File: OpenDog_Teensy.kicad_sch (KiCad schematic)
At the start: 42 parts

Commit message: Added input voltage monitoring cirquit.
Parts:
- added C: C, symbol Device:C
- added D: BAT54S, Package_TO_SOT_SMD:SOT-23, symbol Diode:BAT54S
- added R (x3): R, symbol Device:R
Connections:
- net 3.3V: now also D.2
- net GND: now also C.2, D.1, R.2
- net VIn: now also R.1
- net EXT8: no longer names the net of J.10 (Pin_10)
- net EXT8: no longer U.33 (41_A17)
- new net: C.1, D.3, R.1, R.2, R.2
- new net V_MON: R.1, U.33 (41_A17)
- no-connect marks 7 -> 8

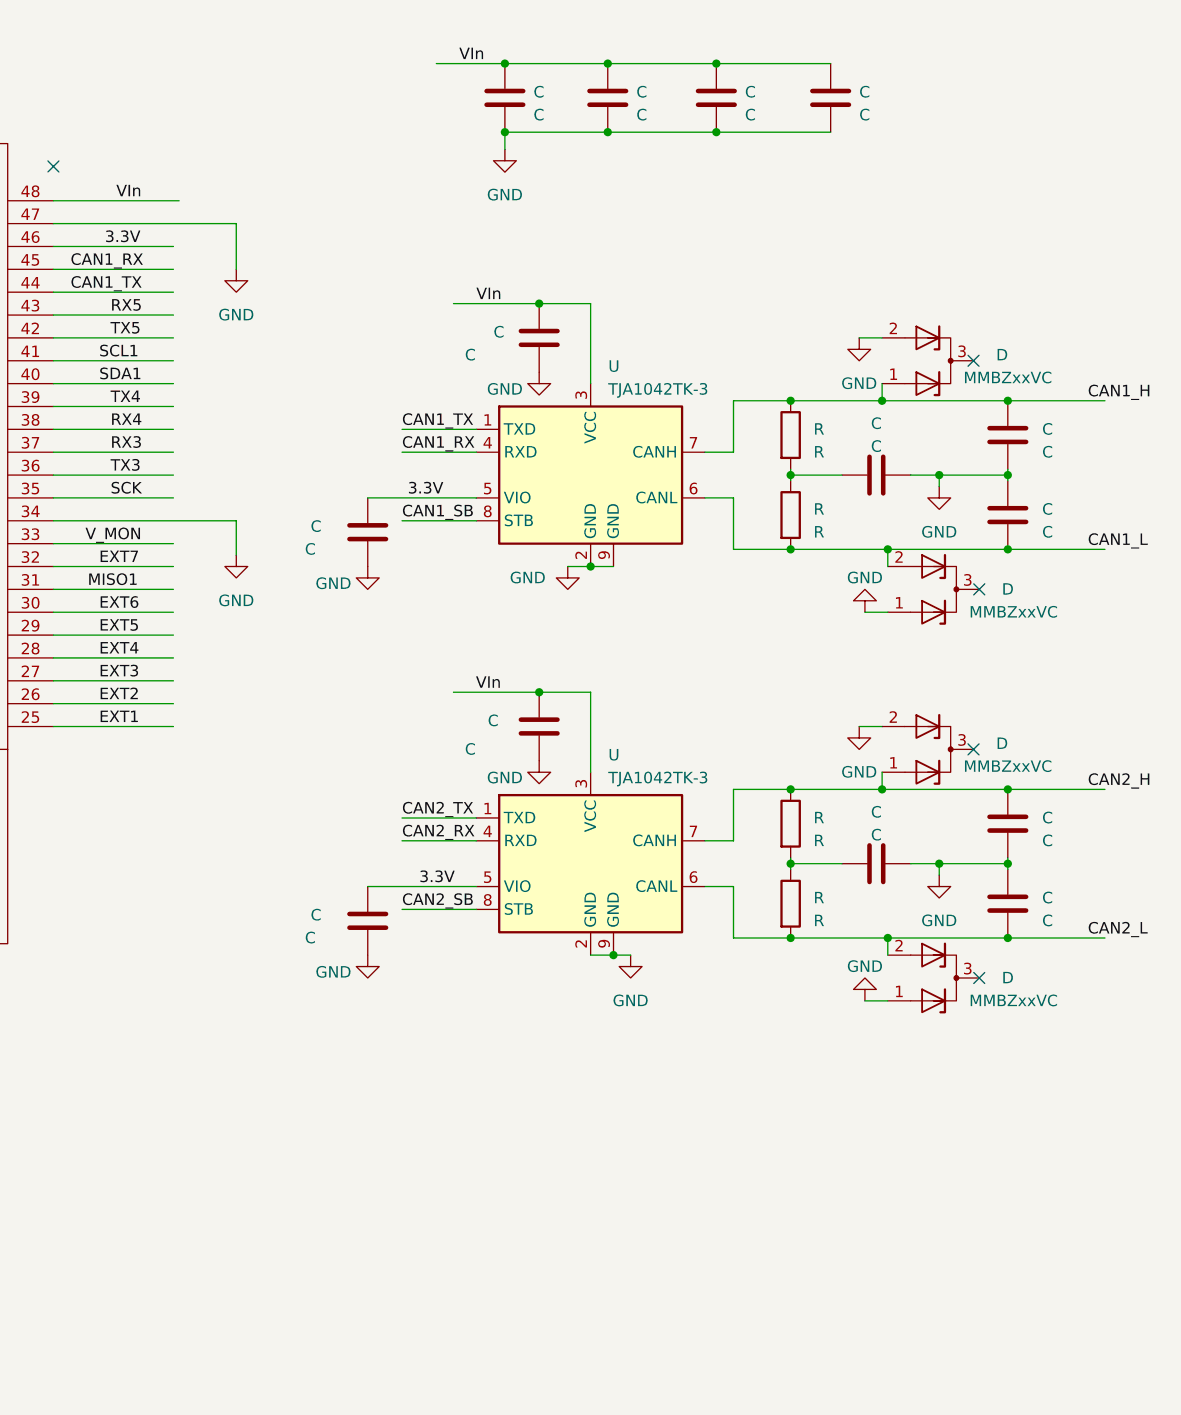
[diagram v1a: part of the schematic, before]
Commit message: Added more filtering capacitors on the 3.3v rail one for each connector.
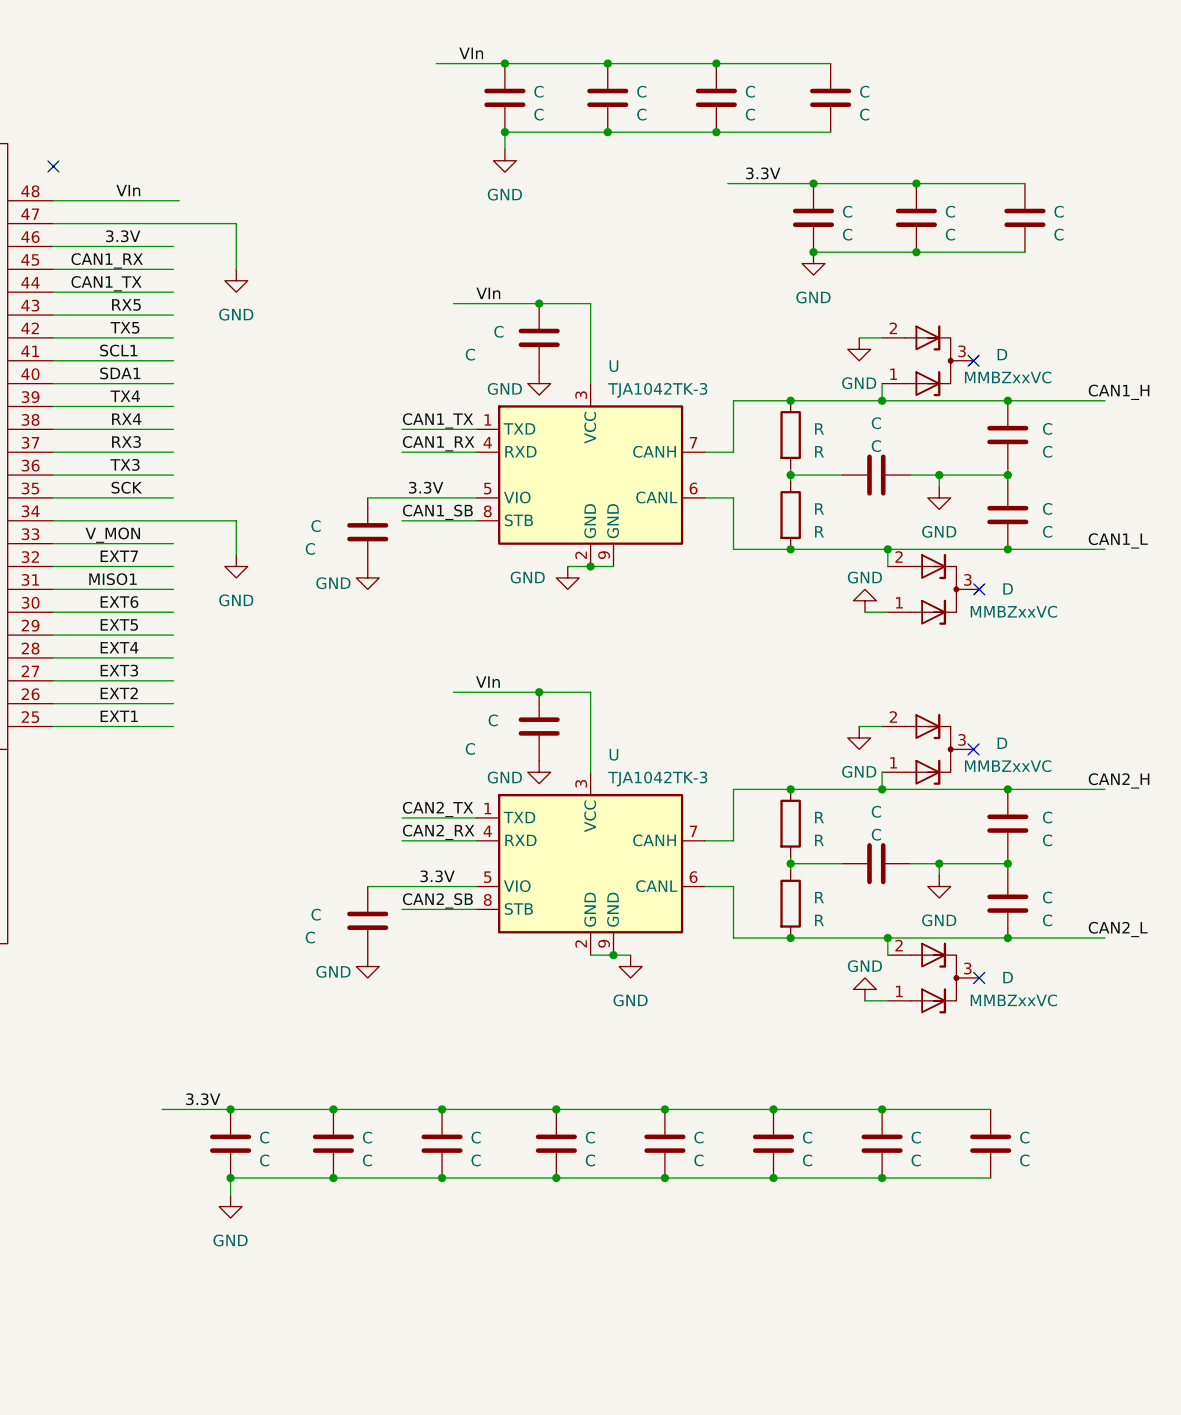
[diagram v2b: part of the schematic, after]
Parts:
- added C (x11): C, symbol Device:C
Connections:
- net 3.3V: now also C.1, C.1, C.1, C.1, C.1, C.1, C.1, C.1, C.1, C.1, C.1
- net GND: now also C.2, C.2, C.2, C.2, C.2, C.2, C.2, C.2, C.2, C.2, C.2

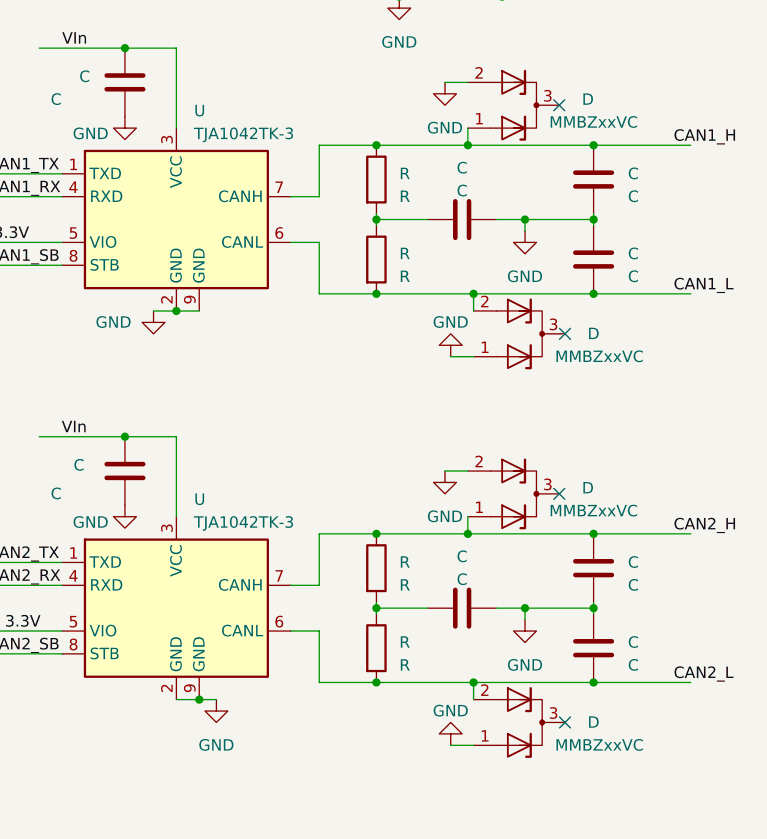
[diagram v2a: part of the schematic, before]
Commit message: Update OpenDog board part numbers. Small routing changes.
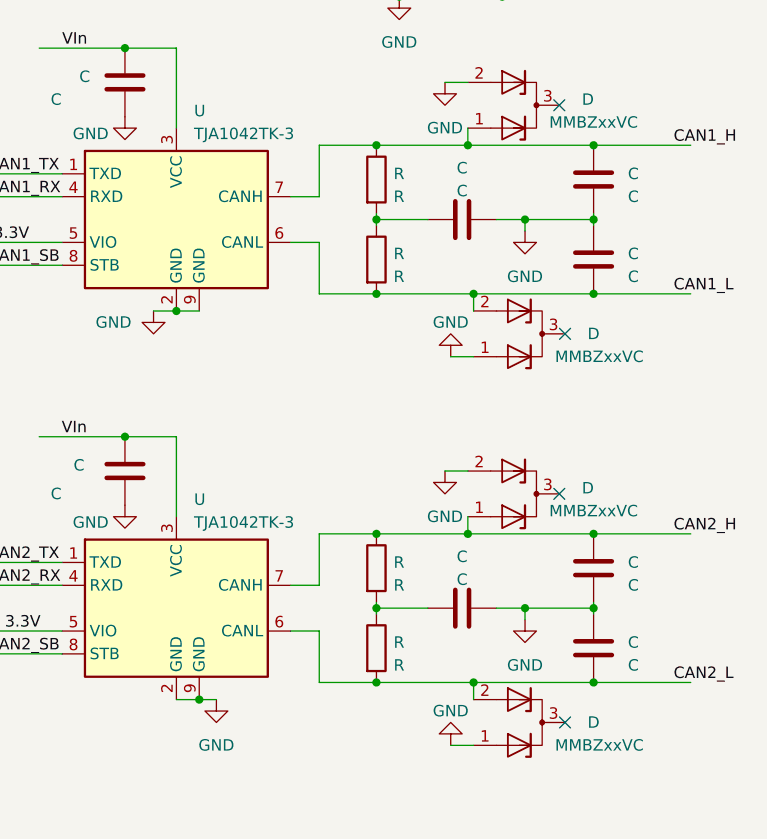
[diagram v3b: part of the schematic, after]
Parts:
- J: JLC Part # C8439 -> C8404
- R: JLC Part # (none) -> C23090
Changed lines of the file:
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@@
       (effects (font (size 1.27 1.27)) hide)
     )
-    (property "JLC Part #" "C8439" (id 4) (at 30.48 183.515 0)
+    (property "JLC Part #" "C8404" (id 4) (at 30.48 183.515 0)
       (effects (font (size 1.27 1.27)) hide)
     )
@@
     (in_bom yes) (on_board yes) (fields_autoplaced)
     (default_instance (reference "R") (unit 1) (value "R") (footprint ""))
-    (property "Reference" "R" (id 0) (at 240.665 119.38 0)
-      (effects (font (size 1.27 1.27)) (justify left))
-    )
-    (property "Value" "R" (id 1) (at 240.665 121.92 0)
+    (property "Reference" "R" (id 0) (at 240.03 119.38 0)
+      (effects (font (size 1.27 1.27)) (justify left))
+    )
+    (property "Value" "R" (id 1) (at 240.03 121.92 0)
       (effects (font (size 1.27 1.27)) (justify left))
     )
@@
     )
     (property "Datasheet" "~" (id 3) (at 238.125 120.015 0)
+      (effects (font (size 1.27 1.27)) hide)
+    )
+    (property "JLC Part #" "C23090" (id 4) (at 238.125 120.015 0)
       (effects (font (size 1.27 1.27)) hide)
     )
@@
     (in_bom yes) (on_board yes) (fields_autoplaced)
     (default_instance (reference "R") (unit 1) (value "R") (footprint ""))
-    (property "Reference" "R" (id 0) (at 240.665 110.49 0)
-      (effects (font (size 1.27 1.27)) (justify left))
-    )
-    (property "Value" "R" (id 1) (at 240.665 113.03 0)
+    (property "Reference" "R" (id 0) (at 240.03 110.49 0)
+      (effects (font (size 1.27 1.27)) (justify left))
+    )
+    (property "Value" "R" (id 1) (at 240.03 113.03 0)
       (effects (font (size 1.27 1.27)) (justify left))
     )
@@
     )
     (property "Datasheet" "~" (id 3) (at 238.125 111.125 0)
+      (effects (font (size 1.27 1.27)) hide)
+    )
+    (property "JLC Part #" "C23090" (id 4) (at 238.125 111.125 0)
       (effects (font (size 1.27 1.27)) hide)
     )
@@
     (in_bom yes) (on_board yes) (fields_autoplaced)
     (default_instance (reference "R") (unit 1) (value "R") (footprint ""))
-    (property "Reference" "R" (id 0) (at 240.665 76.2 0)
-      (effects (font (size 1.27 1.27)) (justify left))
-    )
-    (property "Value" "R" (id 1) (at 240.665 78.74 0)
+    (property "Reference" "R" (id 0) (at 240.03 76.2 0)
+      (effects (font (size 1.27 1.27)) (justify left))
+    )
+    (property "Value" "R" (id 1) (at 240.03 78.74 0)
       (effects (font (size 1.27 1.27)) (justify left))
     )
@@
       (effects (font (size 1.27 1.27)) hide)
     )
+    (property "JLC Part #" "C23090" (id 4) (at 238.125 76.835 0)
+      (effects (font (size 1.27 1.27)) hide)
+    )
     (pin "1")
     (pin "2")
@@
     (in_bom yes) (on_board yes) (fields_autoplaced)
     (default_instance (reference "R") (unit 1) (value "R") (footprint ""))
-    (property "Reference" "R" (id 0) (at 240.665 67.31 0)
-      (effects (font (size 1.27 1.27)) (justify left))
-    )
-    (property "Value" "R" (id 1) (at 240.665 69.85 0)
+    (property "Reference" "R" (id 0) (at 240.03 67.31 0)
+      (effects (font (size 1.27 1.27)) (justify left))
+    )
+    (property "Value" "R" (id 1) (at 240.03 69.85 0)
       (effects (font (size 1.27 1.27)) (justify left))
     )
@@
     )
     (property "Datasheet" "~" (id 3) (at 238.125 67.945 0)
+      (effects (font (size 1.27 1.27)) hide)
+    )
+    (property "JLC Part #" "C23090" (id 4) (at 238.125 67.945 0)
       (effects (font (size 1.27 1.27)) hide)
     )
@@
     )
     (path "/f20f5656-102e-41f9-ba3f-0e35d3dd3685"
-      (reference "R1") (unit 1) (value "60") (footprint "Resistor_SMD:R_0603_1608Metric")
+      (reference "R1") (unit 1) (value "60.4") (footprint "Resistor_SMD:R_0603_1608Metric")
     )
     (path "/efaf3c9b-d52f-4b7f-9918-cc8d377339a2"
-      (reference "R2") (unit 1) (value "60") (footprint "Resistor_SMD:R_0603_1608Metric")
+      (reference "R2") (unit 1) (value "60.4") (footprint "Resistor_SMD:R_0603_1608Metric")
     )
     (path "/bbc7a7e2-69f6-4f38-ae6b-36933a3e619a"
-      (reference "R3") (unit 1) (value "60") (footprint "Resistor_SMD:R_0603_1608Metric")
+      (reference "R3") (unit 1) (value "60.4") (footprint "Resistor_SMD:R_0603_1608Metric")
     )
     (path "/9e4193a8-3a88-4c5a-abef-e956b2dbe67d"
-      (reference "R4") (unit 1) (value "60") (footprint "Resistor_SMD:R_0603_1608Metric")
+      (reference "R4") (unit 1) (value "60.4") (footprint "Resistor_SMD:R_0603_1608Metric")
     )
     (path "/98190db3-f442-43a2-bcce-947e71ee43d9"

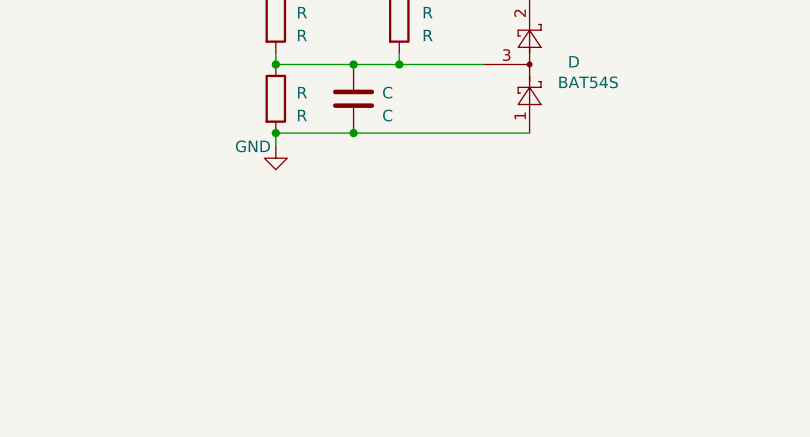
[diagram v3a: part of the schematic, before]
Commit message: Added I2C pullups to the OpenDog board.
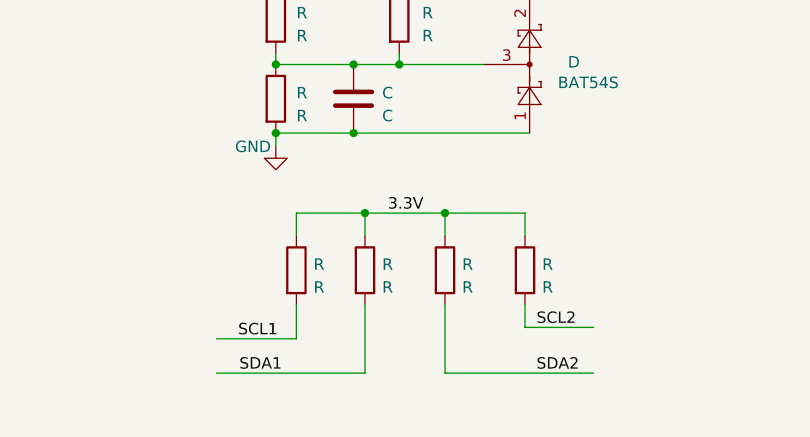
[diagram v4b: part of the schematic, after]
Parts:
- added R (x4): R, symbol Device:R
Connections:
- net 3.3V: now also R.1, R.1, R.1, R.1
- net SCL1: now also R.2
- net SCL2: now also R.2
- net SDA1: now also R.2
- net SDA2: now also R.2

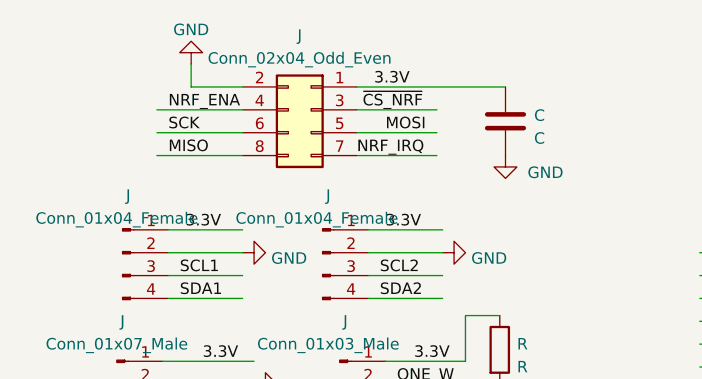
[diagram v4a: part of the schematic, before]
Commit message: Fixed NRF connector pinout.
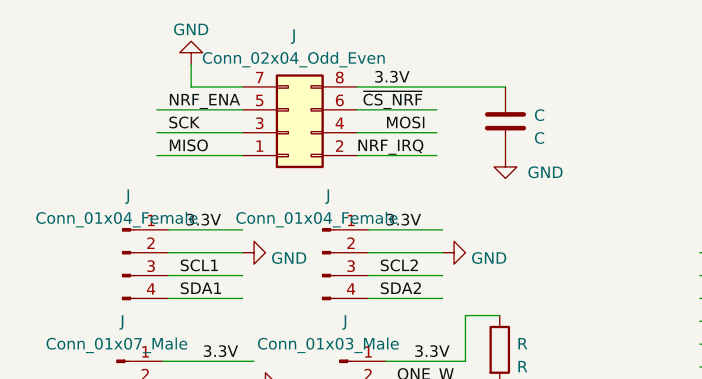
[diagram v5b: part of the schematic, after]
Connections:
- net 3.3V: now also J.8 (Pin_8); no longer J.1 (Pin_1)
- net GND: now also J.7 (Pin_7); no longer J.2 (Pin_2)
- net MISO: now also J.1 (Pin_1); no longer J.8 (Pin_8)
- net MOSI: now also J.4 (Pin_4); no longer J.5 (Pin_5)
- net NRF_ENA: now also J.5 (Pin_5); no longer J.4 (Pin_4)
- net NRF_IRQ: now also J.2 (Pin_2); no longer J.7 (Pin_7)
- net SCK: now also J.3 (Pin_3); no longer J.6 (Pin_6)
- net ~{CS_NRF}: now also J.6 (Pin_6); no longer J.3 (Pin_3)
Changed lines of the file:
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@@
     (pin "2")
   )
-  (symbol (lib_id "Connector_Generic:Conn_02x04_Odd_Even") (at 45.72 28.575 0) (mirror y) (unit 1)
+  (symbol (lib_id "Connector_Generic:Conn_02x04_Odd_Even") (at 43.18 31.115 0) (mirror x) (unit 1)
     (in_bom yes) (on_board yes)
     (default_instance (reference "J") (unit 1) (value "Conn_02x04_Odd_Even") (footprint ""))
-    (property "Reference" "J" (id 0) (at 44.45 20.32 0)
+    (property "Reference" "J" (id 0) (at 43.815 20.32 0)
       (effects (font (size 1.27 1.27)))
     )
-    (property "Value" "Conn_02x04_Odd_Even" (id 1) (at 44.45 22.86 0)
+    (property "Value" "Conn_02x04_Odd_Even" (id 1) (at 43.815 22.86 0)
       (effects (font (size 1.27 1.27)))
     )
-    (property "Footprint" "" (id 2) (at 45.72 28.575 0)
+    (property "Footprint" "" (id 2) (at 43.18 31.115 0)
       (effects (font (size 1.27 1.27)) hide)
     )
-    (property "Datasheet" "~" (id 3) (at 45.72 28.575 0)
+    (property "Datasheet" "~" (id 3) (at 43.18 31.115 0)
       (effects (font (size 1.27 1.27)) hide)
     )
-    (property "JLC Part #" "C2834799" (id 4) (at 45.72 28.575 0)
+    (property "JLC Part #" "C2834799" (id 4) (at 43.18 31.115 0)
       (effects (font (size 1.27 1.27)) hide)
     )
